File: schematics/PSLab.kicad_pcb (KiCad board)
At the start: 4 copper layers, 99 x 53.3 mm, 160 parts, among them CON1 USB-MINI-B, J1 Programmer, J10 GND, J11 Vbus, J13 D+, J14 D-, J16 I2C-2, J2 DoublePins, J3 LA, J4 Outputs, J5 Bluetooth, J6 I2C-1, J7 UART/ESP, J8 Power Pins, Q1 MMBT3906, Q2 MMBT3904, Q3 MMBT3906, U1 MCP2200, U10 TL082, U11 6S21, U12 6S21, U13 TL082, U15 ESP8266, U16 TL082, U2 74HC126, U3 PIC24EP256GP204, U4 TC1240A, U5 7660, U6 LM1117-3.3, U7 LM324, U8 TL082, U9 MCP4728, X1 12MHz, Y1 12MHz

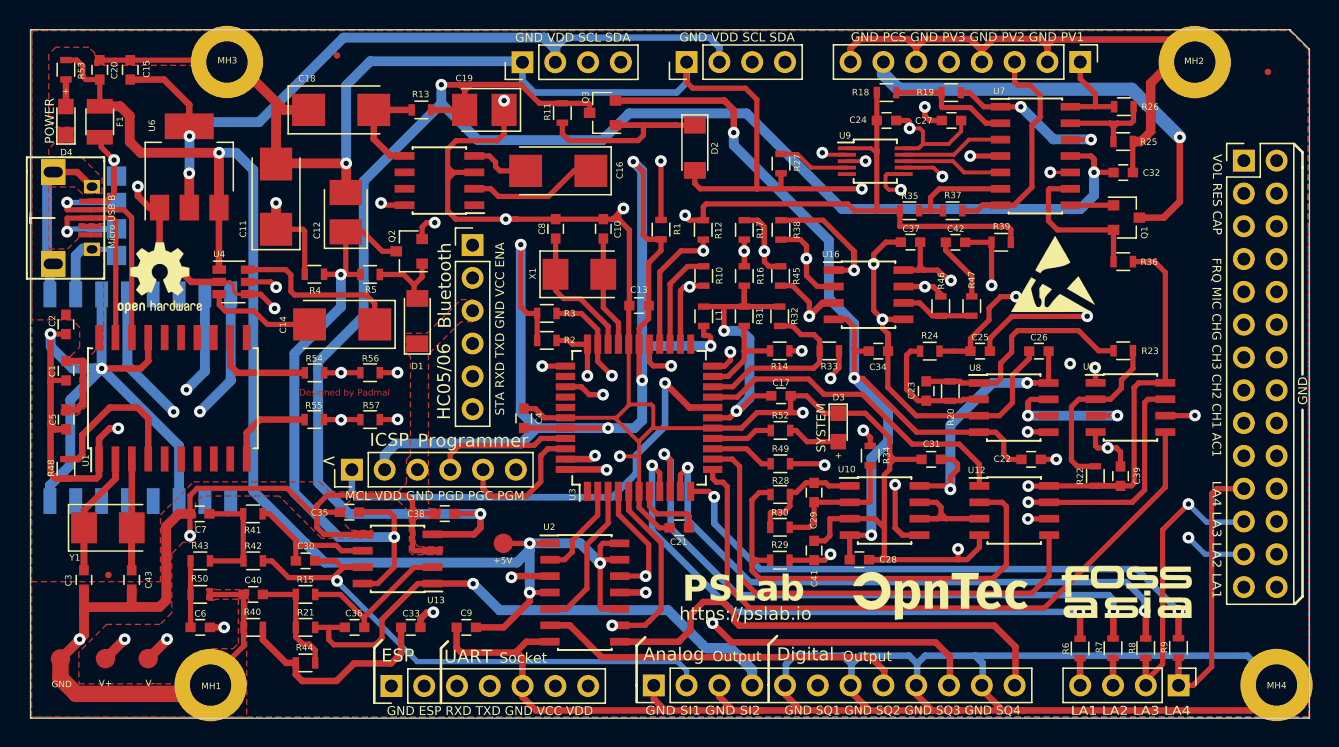
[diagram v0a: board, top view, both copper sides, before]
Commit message: Optimized Routing and Fixed DRC
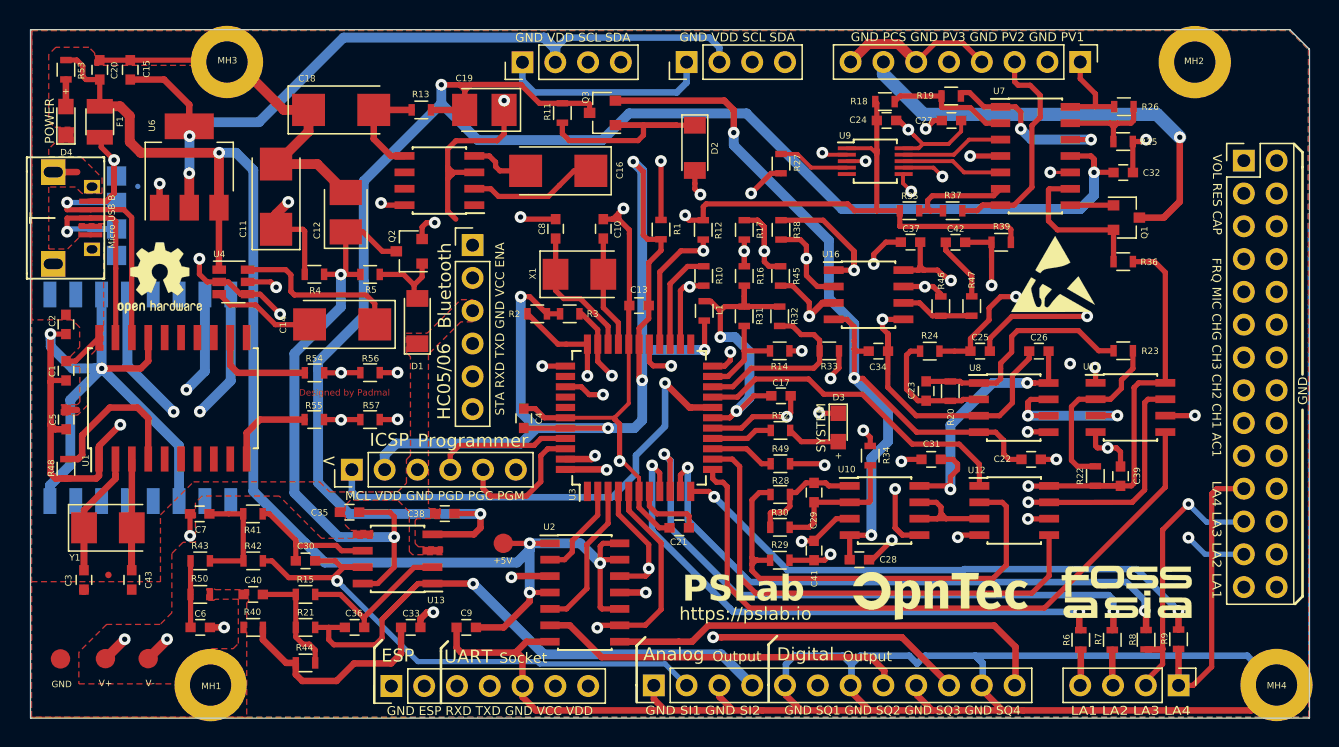
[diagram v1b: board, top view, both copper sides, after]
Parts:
- removed TP5, TP7: Fiducial, Fiducials:Fiducial_0.5mm_Dia_1mm_Outer
- moved R2 2.19 mm to (130.2, 82.3), turned to 0 degrees
- moved R3 1.77 mm to (132.7, 82.3)
- moved R18 0.71 mm to (157.1, 65.8)
- moved R9 0.67 mm to (179.8, 107.5)
- moved R6 0.66 mm to (172.3, 107.5)
- moved R8 0.65 mm to (177.3, 107.5)
- moved R7 0.64 mm to (174.7, 107.5)
- moved L1 0.42 mm to (143.1, 82.0)
- moved R19 0.26 mm to (162.2, 65.4)
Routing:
- net GND: track 777.3 -> 363.3 mm, vias 18 -> 23
- net Vdd: track 314.1 -> 305.4 mm
- net SINE2: track 53.5 -> 47.3 mm
- net V+: track 147.1 -> 141.1 mm
- net SCL: track 64.5 -> 67.6 mm
- net /ID2: track 51.3 -> 48.6 mm
- net /I/O Processing/DAC4: track 17.3 -> 14.6 mm
- net SQR4: track 37.4 -> 34.9 mm
- net /D+: track 22.3 -> 20.2 mm
- net SDA: track 68.6 -> 66.7 mm
- net /ID4: track 44.9 -> 43.1 mm
- net SQ4: track 50.1 -> 48.5 mm
- net SQR3: track 29.8 -> 28.5 mm
- net Net-(R16-Pad1): track 52.2 -> 51.2 mm
- net SQ3: track 30.5 -> 29.6 mm
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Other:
- board text removed: "Square Wave 3"

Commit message: Optimized Routing
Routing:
- net GND: track 363.3 -> 315.3 mm, vias 23 -> 22
- net TxD: track 73.3 -> 67.9 mm
- net Vdd: track 305.4 -> 301.0 mm
- net IDA: track 22.8 -> 18.6 mm
- net /ID4: track 43.1 -> 46.2 mm
- net /ID1: track 44.6 -> 47.0 mm
- net IDD: track 22.1 -> 20.2 mm
- net SQR3: track 28.5 -> 30.0 mm
- net /ID2: track 48.6 -> 49.8 mm
- net MIC: track 25.7 -> 24.6 mm
- net /ID3: track 46.5 -> 45.6 mm
- net RxD: track 69.8 -> 68.9 mm
